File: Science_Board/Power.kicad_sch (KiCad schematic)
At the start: 50 parts, among them IC1 TCKE603RA, IC2 TCKE603RA, IC3 TCKE603RM, J21 Molex_Megafit_02, J3 Molex_Megafit_02, J4 Molex_Megafit_02, Q1 BS250, Q2 NMOS, Q3 NMOS, Q4 NMOS, U1 AP63205WU

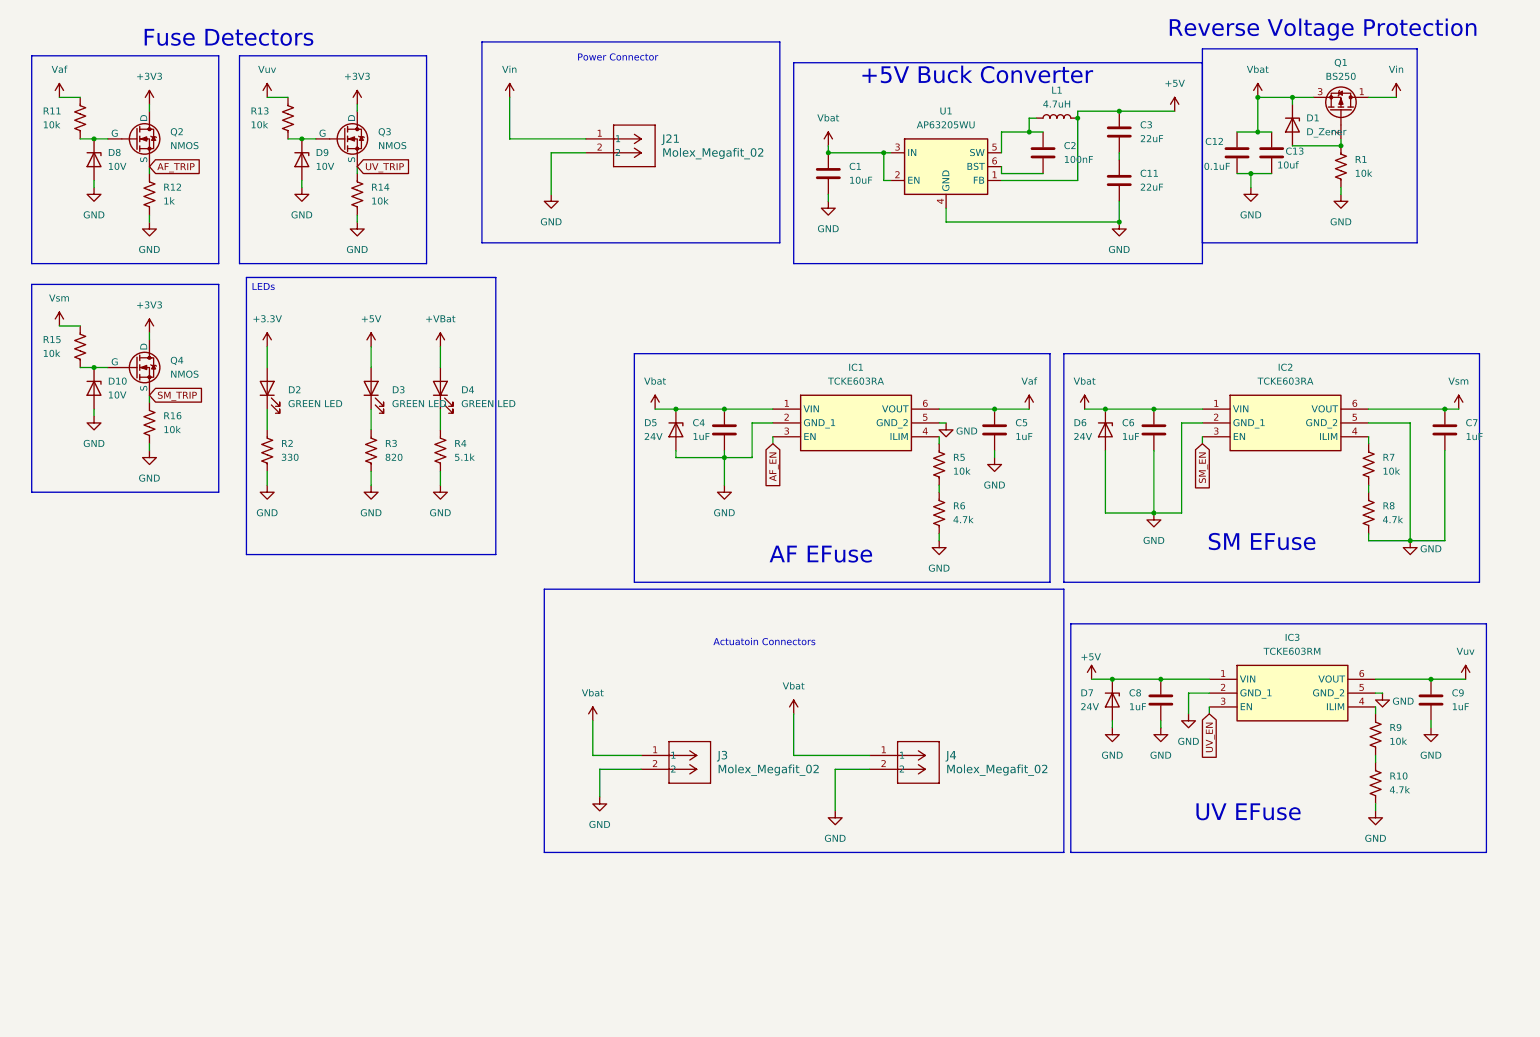
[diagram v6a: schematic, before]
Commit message: Fixed more like changing Vbat to +PV
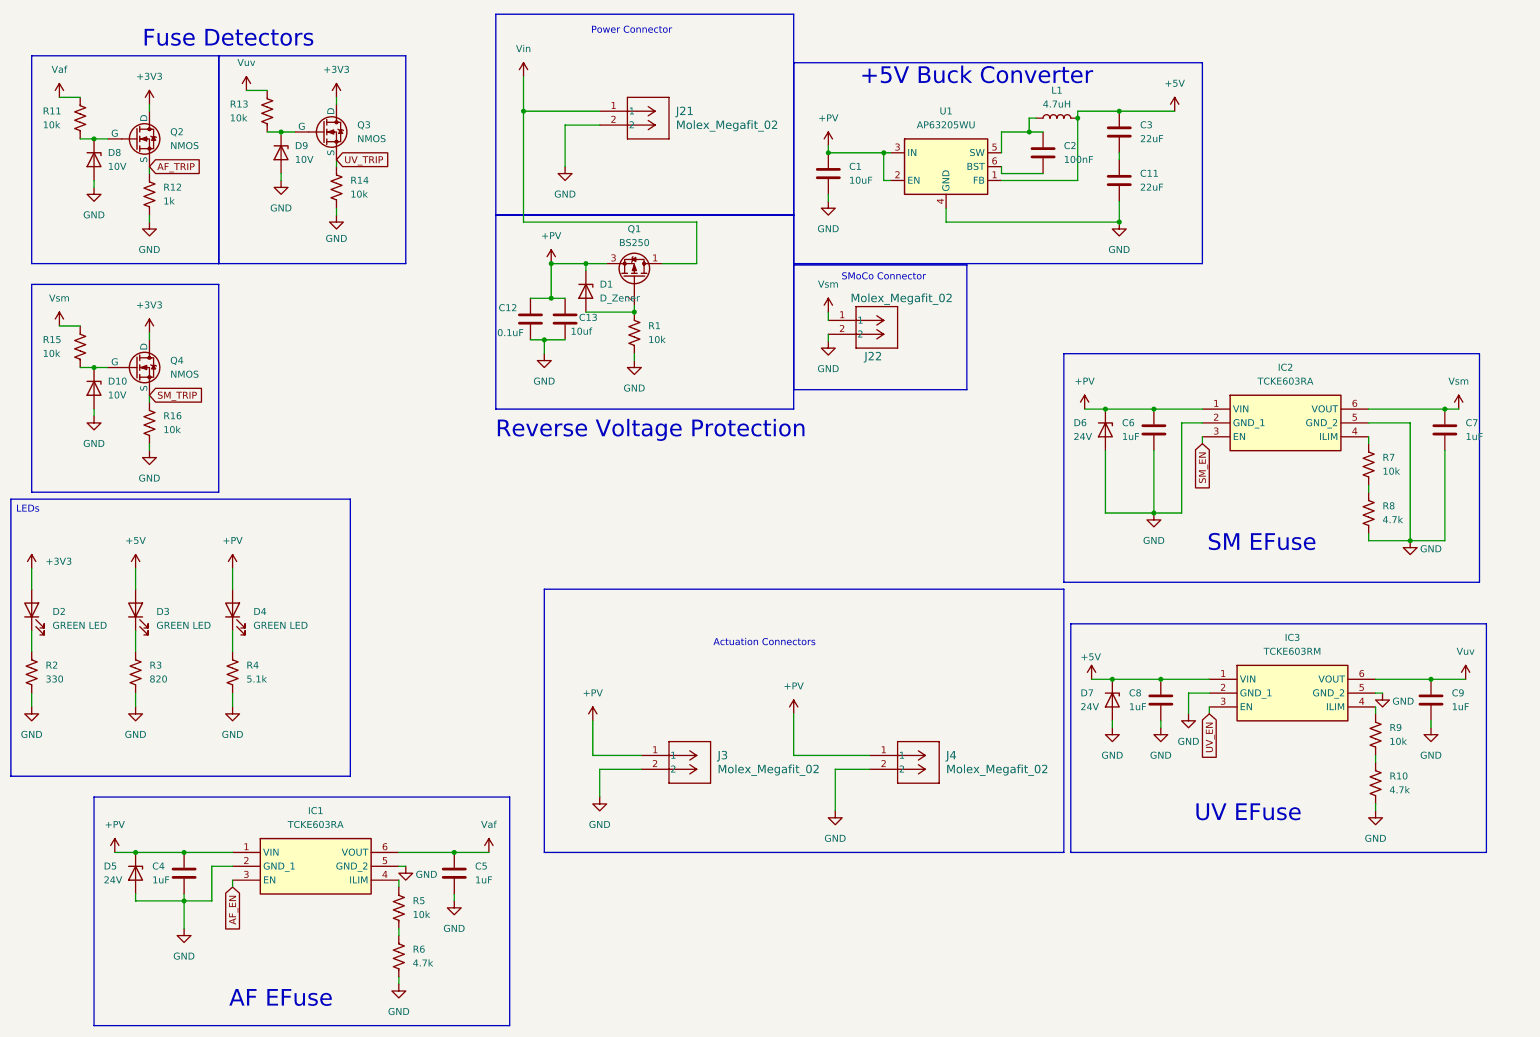
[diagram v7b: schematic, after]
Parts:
- added J22: Molex_Megafit_02, MRDT_Connectors:MOLEX_MegaFit_02_Horizontal, symbol MRDT_Connectors:Molex_Megafit_02
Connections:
- net +3.3V is gone; now on net +3V3: D2.2 (A)
- net Vbat is gone; now on net +PV: C1.1, C12.1, C13.2, C4.1, C6.1, D1.1 (K), D5.1 (K), D6.1 (K), IC1.1 (VIN), IC2.1 (VIN), J3.1, J4.1, Q1.3 (S), U1.2 (EN), U1.3 (IN)
- net GND: now also J22.2
- net Vsm: now also J22.1
- net +VBat renamed +PV
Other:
- note added: "Actuation Connectors"
- note added: "SMoCo Connector"
- note removed: "Actuatoin Connectors"
- moved on the sheet: C12, C13, C4, C5, D1, D2, D3, D4, D5, D9, IC1, J21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

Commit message: Changed footprint of resistors inductors and capacitors
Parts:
- C1, C11, C2, C3: footprint Package_SO:SOIC-8_3.9x4.9mm_P1.27mm -> Capacitor_SMD:C_0603_1608Metric_Pad1.08x0.95mm_HandSolder
- C12, C13: footprint (none) -> Capacitor_SMD:C_0603_1608Metric_Pad1.08x0.95mm_HandSolder
- D1: value D_Zener -> 10V
- D5, D6: value 24V -> 28V
- D7: value 24V -> 6V
- L1: footprint Relay_THT:Relay_DPDT_Finder_30.22 -> Inductor_SMD:L_0603_1608Metric_Pad1.05x0.95mm_HandSolder
- R1, R2, R3, R4: footprint Package_DIP:DIP-8_W7.62mm -> Resistor_SMD:R_0603_1608Metric_Pad0.98x0.95mm_HandSolder
- R10, R6, R8: footprint Package_QFP:LQFP-100_14x14mm_P0.5mm -> Resistor_SMD:R_0603_1608Metric_Pad0.98x0.95mm_HandSolder
- R5, R7, R9: footprint Resistor_SMD:R_0603_1608Metric -> Resistor_SMD:R_0603_1608Metric_Pad0.98x0.95mm_HandSolder
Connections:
- net Vin: no longer names the net of J21.1, Q1.1 (D)
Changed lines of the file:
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@@
 	)
 	(junction
-		(at 106.68 30.48)
-		(diameter 0)
-		(color 0 0 0 0)
-	)
-	(junction
 		(at 118.11 58.42)
 		(diameter 0)
@@
 	(wire
 		(pts
-			(xy 106.68 50.8) (xy 106.68 30.48)
-		)
-		(stroke
-			(width 0)
-			(type default)
-		)
-	)
-	(wire
-		(pts
 			(xy 38.1 29.21) (xy 38.1 30.48)
 		)
@@
 	(wire
 		(pts
+			(xy 106.68 30.48) (xy 106.68 50.8)
+		)
+		(stroke
+			(width 0)
+			(type default)
+		)
+	)
+	(wire
+		(pts
 			(xy 231.14 87.63) (xy 227.33 87.63)
 		)
@@
 	(wire
 		(pts
-			(xy 106.68 24.13) (xy 106.68 30.48)
-		)
-		(stroke
-			(width 0)
-			(type default)
-		)
-	)
-	(wire
-		(pts
 			(xy 83.82 171.45) (xy 83.82 172.72)
 		)
@@
 			)
 		)
-		(property "Footprint" ""
+		(property "Footprint" "Capacitor_SMD:C_0603_1608Metric_Pad1.08x0.95mm_HandSolder"
 			(at 113.3348 64.77 0)
 			(hide yes)
@@
 			)
 		)
-		(property "Footprint" "Package_DIP:DIP-8_W7.62mm"
+		(property "Footprint" "Resistor_SMD:R_0603_1608Metric_Pad0.98x0.95mm_HandSolder"
 			(at 54.356 133.604 90)
 			(hide yes)
@@
 			)
 		)
-		(property "Value" "24V"
+		(property "Value" "28V"
 			(at 207.518 90.17 90)
 			(show_name no)
@@
 			)
 		)
-		(property "Footprint" "Resistor_SMD:R_0603_1608Metric"
+		(property "Footprint" "Resistor_SMD:R_0603_1608Metric_Pad0.98x0.95mm_HandSolder"
 			(at 84.836 176.784 90)
 			(hide yes)
@@
 			)
 		)
-		(property "Footprint" "Package_SO:SOIC-8_3.9x4.9mm_P1.27mm"
+		(property "Footprint" "Capacitor_SMD:C_0603_1608Metric_Pad1.08x0.95mm_HandSolder"
 			(at 216.8652 46.99 0)
 			(hide yes)
@@
 			)
 		)
-		(property "Footprint" "Package_QFP:LQFP-100_14x14mm_P0.5mm"
+		(property "Footprint" "Resistor_SMD:R_0603_1608Metric_Pad0.98x0.95mm_HandSolder"
 			(at 263.906 153.924 90)
 			(hide yes)
@@
 			)
 		)
-		(property "Footprint" ""
+		(property "Footprint" "Capacitor_SMD:C_0603_1608Metric_Pad1.08x0.95mm_HandSolder"
 			(at 108.9152 72.39 0)
 			(hide yes)
@@
 			)
 		)
-		(property "Value" "D_Zener"
+		(property "Value" "10V"
 			(at 120.65 64.7699 90)
 			(show_name no)
@@
 			)
 		)
-		(property "Value" "24V"
+		(property "Value" "6V"
 			(at 208.788 139.7 90)
 			(show_name no)
@@
 			)
 		)
-		(property "Footprint" "Resistor_SMD:R_0603_1608Metric"
+		(property "Footprint" "Resistor_SMD:R_0603_1608Metric_Pad0.98x0.95mm_HandSolder"
 			(at 262.636 95.504 90)
 			(hide yes)
@@
 			)
 		)
-		(property "Footprint" "Package_QFP:LQFP-100_14x14mm_P0.5mm"
+		(property "Footprint" "Resistor_SMD:R_0603_1608Metric_Pad0.98x0.95mm_HandSolder"
 			(at 262.636 104.394 90)
 			(hide yes)
@@
 			)
 		)
-		(property "Footprint" "Package_SO:SOIC-8_3.9x4.9mm_P1.27mm"
+		(property "Footprint" "Capacitor_SMD:C_0603_1608Metric_Pad1.08x0.95mm_HandSolder"
 			(at 216.8652 38.1 0)
 			(hide yes)
@@
 			)
 		)
-		(property "Footprint" "Package_SO:SOIC-8_3.9x4.9mm_P1.27mm"
+		(property "Footprint" "Capacitor_SMD:C_0603_1608Metric_Pad1.08x0.95mm_HandSolder"
 			(at 202.8952 41.91 0)
 			(hide yes)
@@
 			)
 		)
-		(property "Footprint" "Resistor_SMD:R_0603_1608Metric"
+		(property "Footprint" "Resistor_SMD:R_0603_1608Metric_Pad0.98x0.95mm_HandSolder"
 			(at 263.906 145.034 90)
 			(hide yes)
@@
 			)
 		)
-		(property "Footprint" "Package_DIP:DIP-8_W7.62mm"
+		(property "Footprint" "Resistor_SMD:R_0603_1608Metric_Pad0.98x0.95mm_HandSolder"
 			(at 125.984 70.866 90)
 			(hide yes)
@@
 			)
 		)
-		(property "Footprint" "Package_QFP:LQFP-100_14x14mm_P0.5mm"
+		(property "Footprint" "Resistor_SMD:R_0603_1608Metric_Pad0.98x0.95mm_HandSolder"
 			(at 84.836 185.674 90)
 			(hide yes)
@@
 			)
 		)
-		(property "Footprint" "Package_DIP:DIP-8_W7.62mm"
+		(property "Footprint" "Resistor_SMD:R_0603_1608Metric_Pad0.98x0.95mm_HandSolder"
 			(at 36.576 133.604 90)
 			(hide yes)
@@
 			)
 		)
-		(property "Footprint" "Relay_THT:Relay_DPDT_Finder_30.22"
+		(property "Footprint" "Inductor_SMD:L_0603_1608Metric_Pad1.05x0.95mm_HandSolder"
 			(at 204.47 31.75 0)
 			(hide yes)
@@
 	)
 	(symbol
-		(lib_id "power:VCC")
-		(at 106.68 24.13 0)
-		(unit 1)
-		(body_style 1)
-		(exclude_from_sim no)
-		(in_bom yes)
-		(on_board yes)
-		(in_pos_files yes)
-		(dnp no)
-		(fields_autoplaced yes)
-		(property "Reference" "#PWR075"
-			(at 106.68 27.94 0)
-			(hide yes)
-			(show_name no)
-			(do_not_autoplace no)
-			(effects
-				(font
-					(size 1.27 1.27)
-				)
-			)
-		)
-		(property "Value" "Vin"
-			(at 106.68 19.05 0)
-			(show_name no)
-			(do_not_autoplace no)
-			(effects
-				(font
-					(size 1.27 1.27)
-				)
-			)
-		)
-		(property "Footprint" "MRDT_Connectors:MOLEX_MegaFit_02_Horizontal"
-			(at 106.68 24.13 0)
-			(hide yes)
-			(show_name no)
-			(do_not_autoplace no)
-			(effects
-				(font
-					(size 1.27 1.27)
-				)
-			)
-		)
-		(property "Datasheet" ""
-			(at 106.68 24.13 0)
-			(hide yes)
-			(show_name no)
-			(do_not_autoplace no)
-			(effects
-				(font
-					(size 1.27 1.27)
-				)
-			)
-		)
-		(property "Description" "Power symbol creates a global label with name \"VCC\""
-			(at 106.68 24.13 0)
-			(hide yes)
-			(show_name no)
-			(do_not_autoplace no)
-			(effects
-				(font
-					(size 1.27 1.27)
-				)
-			)
-		)
-		(pin "1"
-		)
-		(instances
-			(project "Science_Board"
-				(path "/4f5c5f7f-4385-4de2-96ca-2ae741ebf691/6219bf49-5574-4710-86f4-9f93da84ad76"
-					(reference "#PWR075")
-					(unit 1)
-				)
-			)
-		)
-	)
-	(symbol
 		(lib_id "Device:C")
 		(at 223.52 138.43 0)
@@
 			)
 		)
-		(property "Footprint" "Package_DIP:DIP-8_W7.62mm"
+		(property "Footprint" "Resistor_SMD:R_0603_1608Metric_Pad0.98x0.95mm_HandSolder"
 			(at 17.526 133.604 90)
 			(hide yes)
@@
 			)
 		)
-		(property "Value" "24V"
+		(property "Value" "28V"
 			(at 29.718 171.45 90)
 			(show_name no)
@@
 			)
 		)
-		(property "Footprint" "Package_SO:SOIC-8_3.9x4.9mm_P1.27mm"
+		(property "Footprint" "Capacitor_SMD:C_0603_1608Metric_Pad1.08x0.95mm_HandSolder"
 			(at 163.5252 45.72 0)
 			(hide yes)
